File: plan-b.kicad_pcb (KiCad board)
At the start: 4 copper layers, 82.4 x 70 mm, 77 parts, among them J1 HRO_TYPE-C-31-M-14, J2 Battery, J3 rgb, J4 columns, J5 Conn_01x10, J6 rows, J7 sensor, J8 Conn_ARM_SWD_TagConnect_TC203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, J9 Conn_01x05_Pin, J99 rows, SW1 Battery, SW2 Reset, U1 nRF52840-QIAA, U3 TPS22919DCKR, U4 TPS22919DCKR, X1 32MHz, X2 32.768kHz

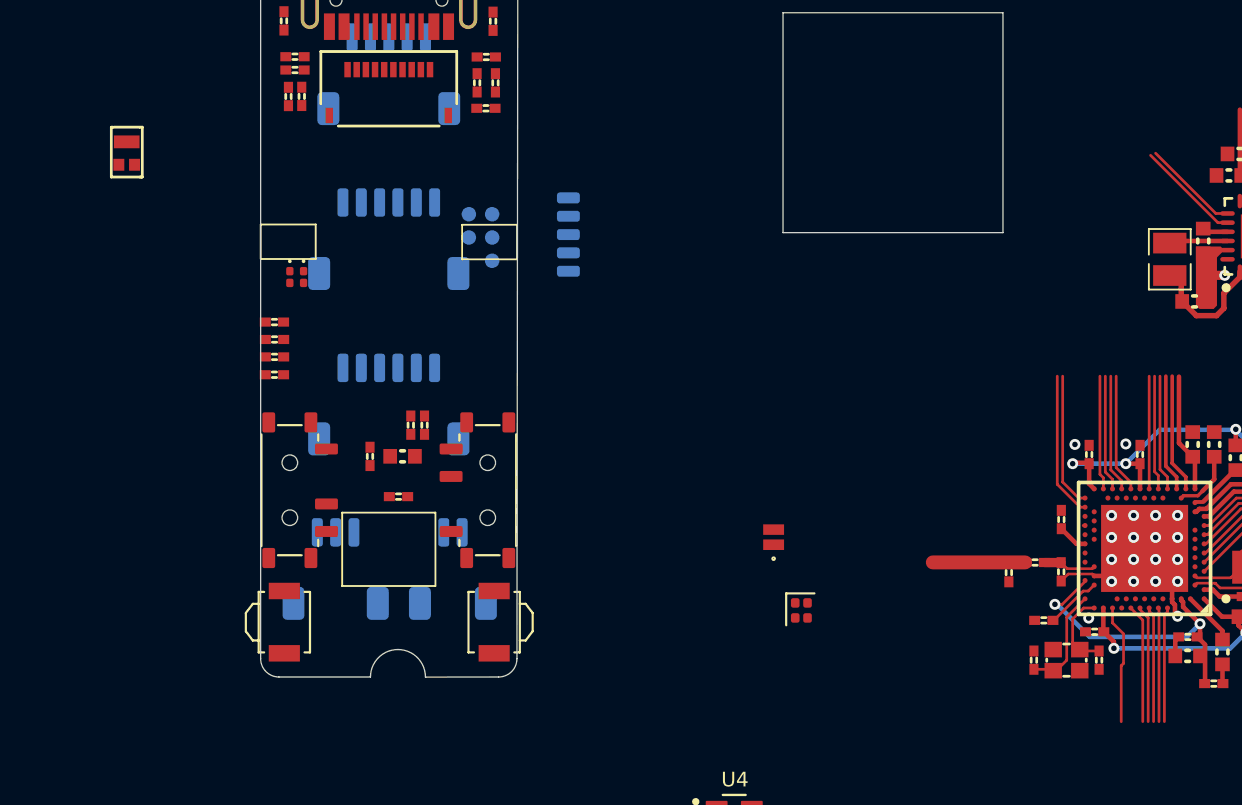
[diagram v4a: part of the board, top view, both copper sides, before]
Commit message: Setting up the RF/Antenna setup
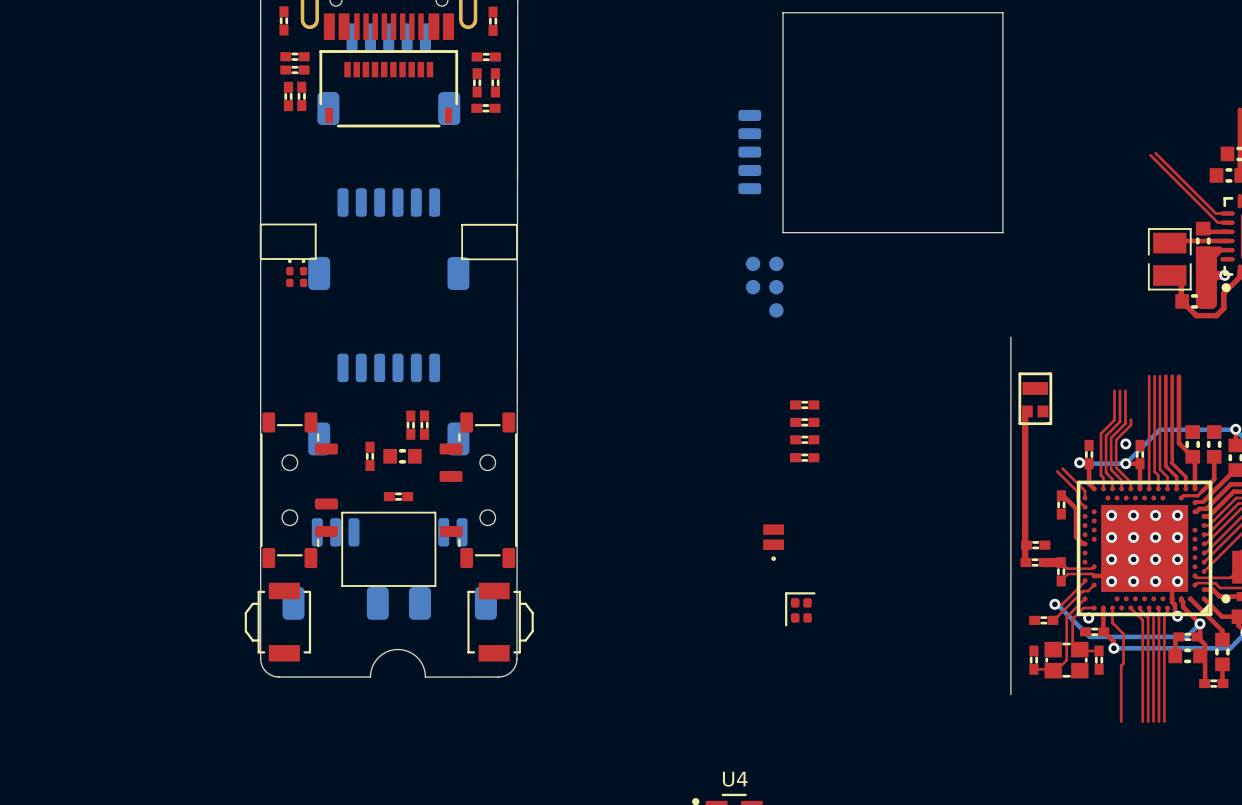
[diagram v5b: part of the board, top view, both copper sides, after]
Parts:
- moved AE1 51.4 mm to (185.3, 84.6)
- moved R11 29.3 mm to (172.7, 84.9)
- moved R14 29.3 mm to (172.7, 85.8)
- moved R15 29.3 mm to (172.7, 86.8)
- moved R16 29.3 mm to (172.7, 87.7)
- moved J8 15.7 mm to (170.5, 78.4)
- moved J9 10.9 mm to (171.4, 71.0)
- moved C4 2.09 mm to (185.3, 92.5), turned to 180 degrees
- moved C9 0.80 mm to (186.7, 90.3), turned to -90 degrees
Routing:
- net SWCLK: track 7.93 -> 2.58 mm
- net SWDIO: track 7.36 -> 2.11 mm
- net /MCU/RF: track 5.04 -> 8.29 mm
- net unconnected-(U1-P0.20-PadAD16): track 6.48 -> 4.44 mm
- net Net-(U1-DEC5): track 1.64 -> 3.39 mm
- net VDD: track 49.1 -> 48.4 mm
- net unconnected-(U1-P1.00-PadAD22): track 6.23 -> 5.71 mm
- net unconnected-(U1-P0.24-PadAD20): track 6.31 -> 5.81 mm
- net GND: vias 26 -> 25
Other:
- outline, holes or cut-outs redrawn

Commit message: Tidying up the PSU block
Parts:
- J99: value rows -> Net tie
- L5: footprint Parts$:INDC2016X10N -> Library:L_0603_1608
- U2: renamed from U1; value nRF52840-QIAA -> nPM1100-QDAx
- moved R3 1.97 mm to (201.0, 72.5), turned to 90 degrees
- moved LD2 1.93 mm to (201.1, 78.3), turned to -90 degrees
- moved R_ICHG 1.45 mm to (201.0, 74.5), turned to 90 degrees
- moved C26 1.00 mm to (193.9, 78.2)
- moved L5 0.84 mm to (193.2, 76.3)
- moved C24 0.13 mm to (196.0, 72.3)
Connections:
- J99 pad 1: Row 0 -> GND
- J99 pad 2: Row 1 -> PVSS
- U2 pad 1: (no net) -> 1.8v
- U2 pad 10: (no net) -> unconnected-(U2-ERR-Pad10)
- U2 pad 11: (no net) -> GND
- U2 pad 12: (no net) -> Net-(U2-ICHG)
- U2 pad 13: (no net) -> unconnected-(U2-NC-Pad13)
- U2 pad 14: (no net) -> Net-(U2-NTC)
- U2 pad 15: (no net) -> VBAT
- U2 pad 16: (no net) -> VSYS
- U2 pad 17: (no net) -> VBUS
- U2 pad 18: (no net) -> unconnected-(U2-NC-Pad18)
- U2 pad 19: (no net) -> D-
- U2 pad 2: (no net) -> GND
- U2 pad 20: (no net) -> D+
- U2 pad 21: (no net) -> Net-(U2-DEC)
- U2 pad 22: (no net) -> Net-(U2-SW)
- U2 pad 23: (no net) -> PVSS
- U2 pad 24: (no net) -> unconnected-(U2-NC-Pad24)
- U2 pad 25: (no net) -> GND
- U2 pad 3: (no net) -> GND
- U2 pad 4: (no net) -> GND
- U2 pad 5: (no net) -> GND
- U2 pad 6: (no net) -> GND
- U2 pad 7: (no net) -> GND
- U2 pad 8: (no net) -> Net-(LD2-C)
- U2 pad 9: (no net) -> unconnected-(U2-VTERM-Pad9)
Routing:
- net (no net): track 11.0 -> 0.00 mm
- net D+: track 6.39 -> 12.1 mm
- net D-: track 6.46 -> 11.7 mm
- net VSYS: track 29.8 -> 27.0 mm
- net 1.8v: track 7.18 -> 5.98 mm
- net Net-(U2-ICHG): track 1.55 -> 0.58 mm
- net Net-(U2-SW): track 2.84 -> 2.17 mm
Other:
- board size 82.4 x 70 mm -> 40.9 x 43 mm

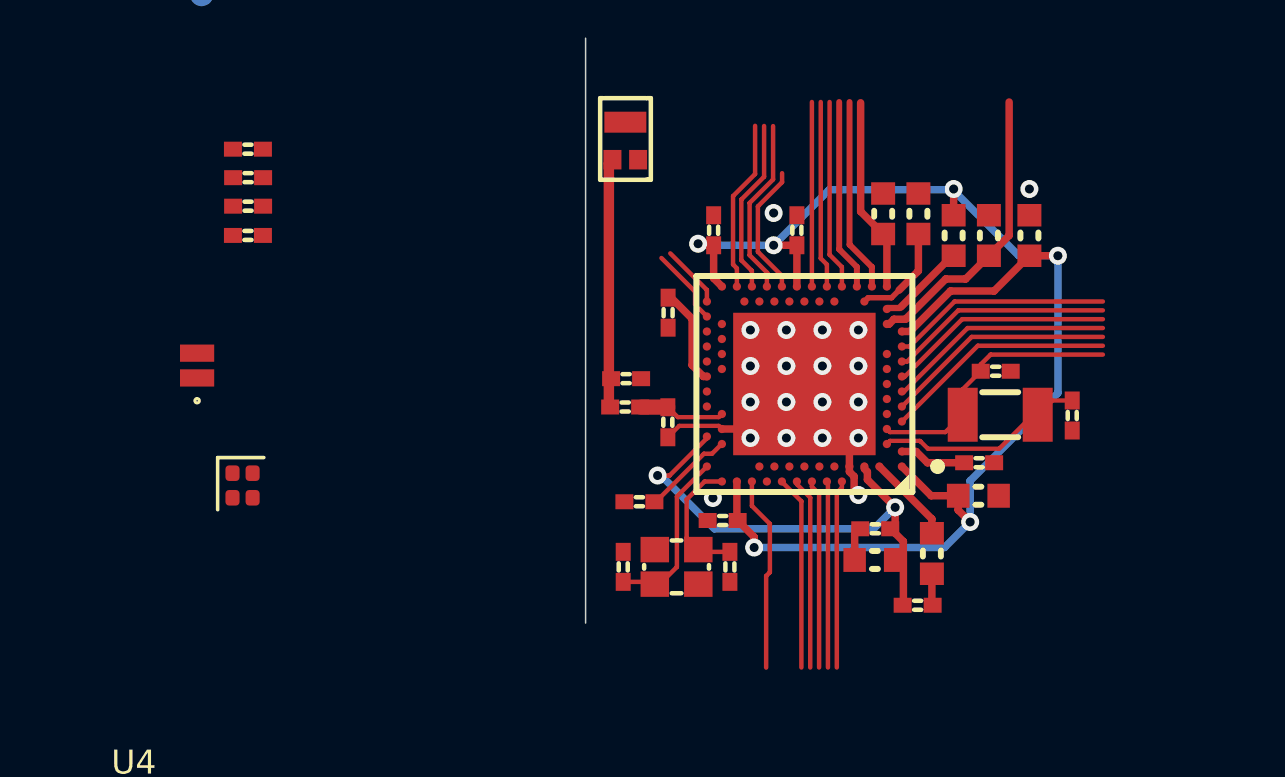
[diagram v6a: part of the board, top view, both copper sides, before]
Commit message: Switching to smaller crystalls
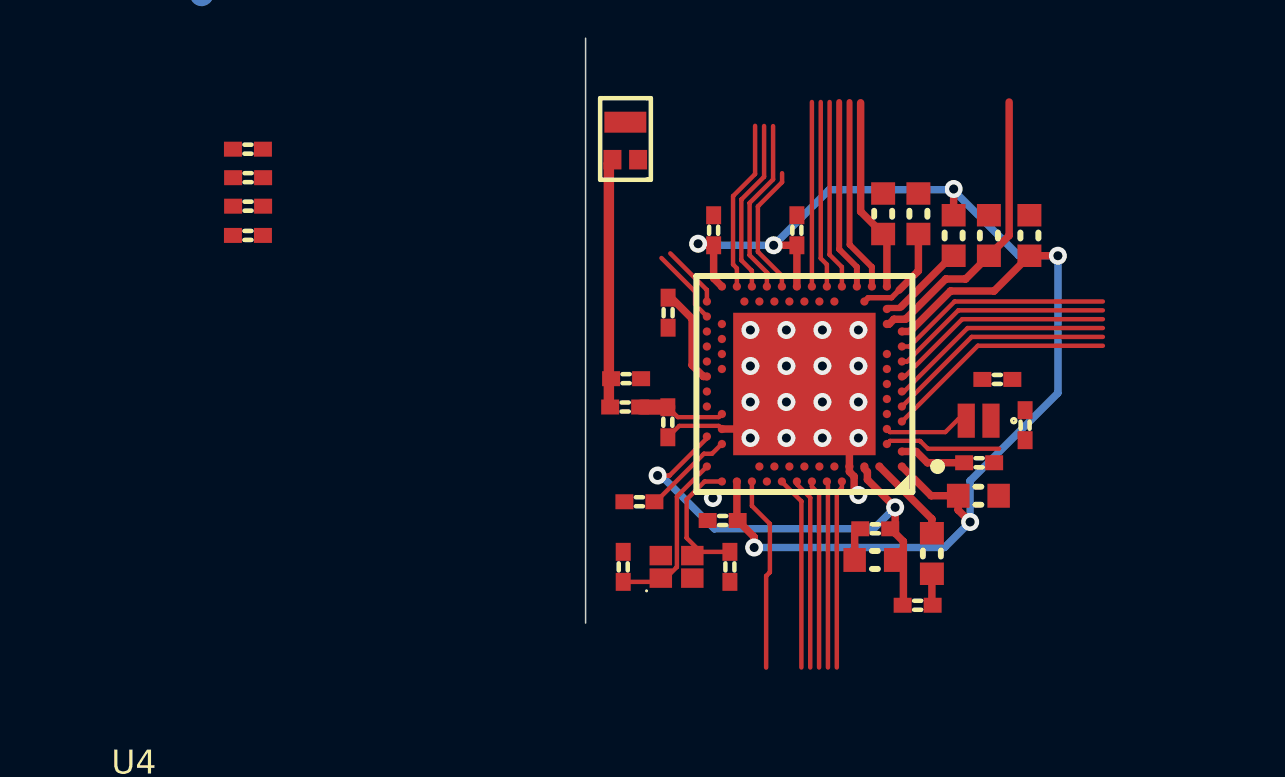
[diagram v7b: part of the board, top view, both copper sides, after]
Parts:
- removed the X1 at (172.5, 96.1)
- removed the X2 at (197.8, 93.7)
- X1: footprint Crystal_Osc$:BT-XTAL_2016 -> NX1612SA-32.000MHZ-CHP:OSCSC105P160X120X35-4N
- moved X2 26.1 mm to (197.1, 93.9), turned to 180 degrees
- moved C17 1.60 mm to (198.6, 94.0)
- moved C18 0.28 mm to (197.7, 92.5)
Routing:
- net Net-(U1-P0.01/XL2): track 8.94 -> 2.83 mm
- net Net-(U1-P0.00/XL1): track 7.00 -> 3.89 mm
- net GND: vias 25 -> 23

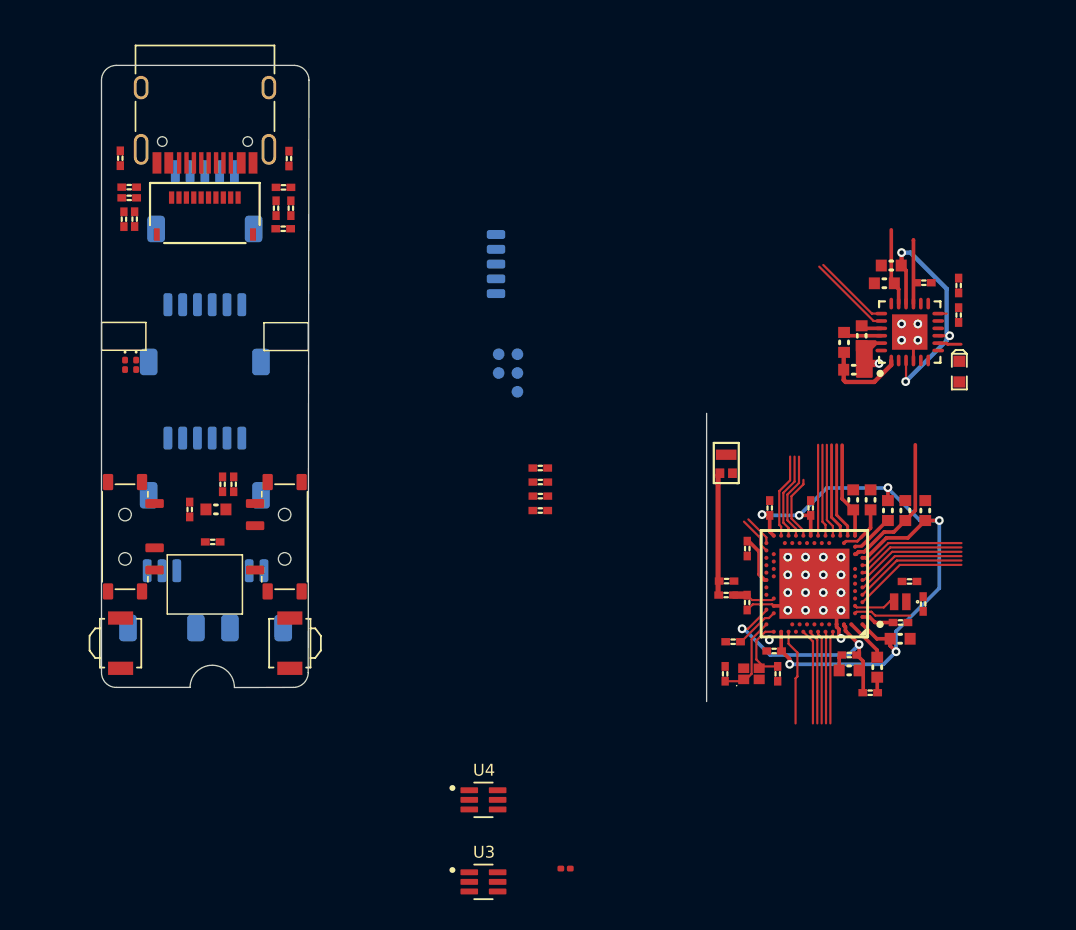
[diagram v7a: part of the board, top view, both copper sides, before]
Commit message: Sorting out the remaining components footprints and rough positioning
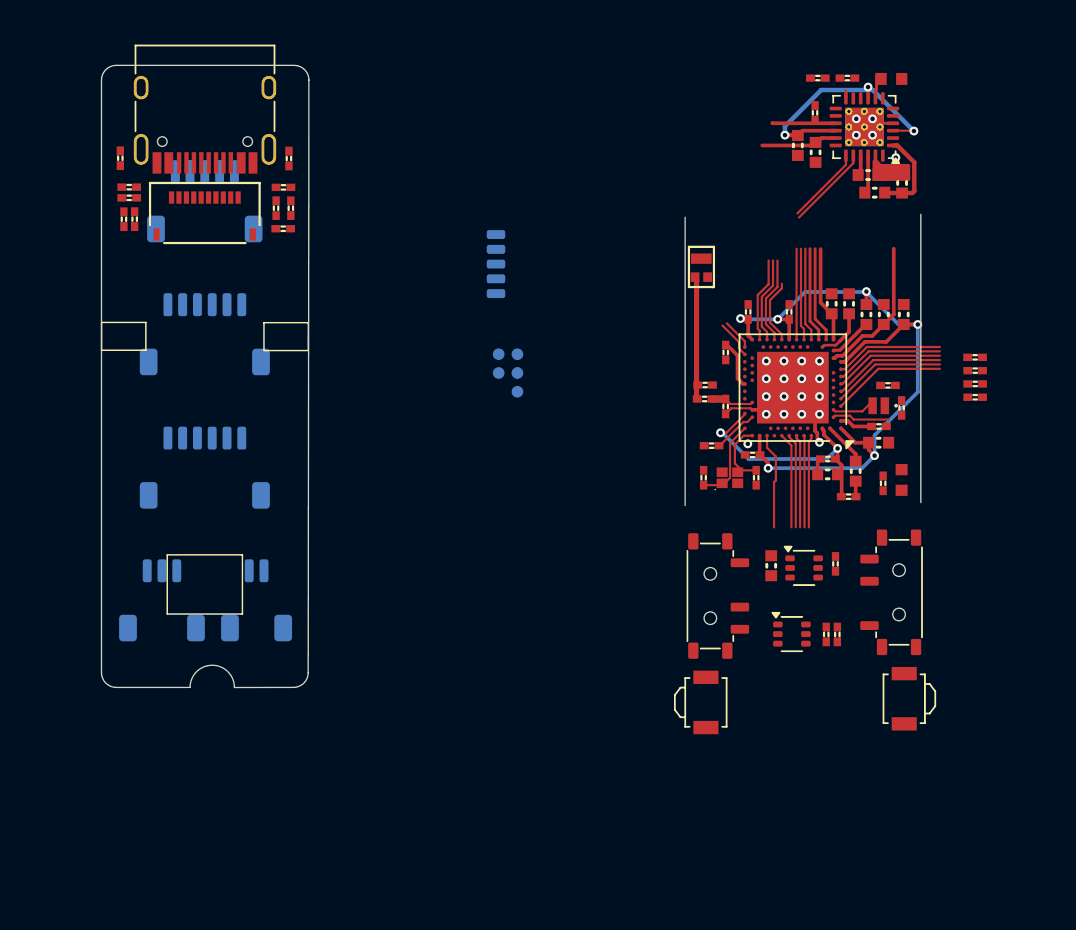
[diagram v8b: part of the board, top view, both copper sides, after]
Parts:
- removed the C22 at (150.5, 89.8)
- removed the LD2 at (145.3, 77.9)
- LD2: footprint pcblib:LED_0603_G -> Library:LED_0603_1608
- LD3: footprint LED_SMD:LED_0201_0603Metric -> Library:LED_0603_1608
- R_BLE1: footprint Resistor_SMD:R_0201_0603Metric -> Library:R_0402_1005
- U1: footprint AQFN50P700X700X85_HS-74N:AQFN50P700X700X85_HS-74N -> Package_DFN_QFN:Nordic_AQFN-73-1EP_7x7mm_P0.5mm
- U2: footprint Parts$:QFN50P400X400X80_HS-25N -> Package_DFN_QFN:QFN-24-1EP_4x4mm_P0.5mm_EP2.6x2.6mm_ThermalVias
- U3, U4: footprint TPS22919:SOT65P210X110-6N -> Package_TO_SOT_SMD:SOT-363_SC-70-6
- moved LD3 53.1 mm to (197.1, 85.7), turned to 90 degrees
- moved R8 43.8 mm to (192.7, 91.3)
- moved R_DIV1 42.1 mm to (192.8, 96.1)
- moved R_DIV2 42.1 mm to (192.0, 96.1)
- moved SW1 41.7 mm to (197.0, 93.3)
- moved SW2 41.7 mm to (197.3, 100.5)
- moved SW1 39.8 mm to (184.2, 93.5)
- moved SW2 39.8 mm to (183.9, 100.7)
- moved C44 37.8 mm to (188.3, 91.5), turned to 90 degrees
- moved R_BLE1 33.8 mm to (195.9, 85.9), turned to 90 degrees
- moved R16 30.4 mm to (202.1, 80.1)
- moved R15 30.4 mm to (202.1, 79.2)
- moved R14 30.4 mm to (202.1, 78.3)
- moved R11 30.4 mm to (202.1, 77.4)
- moved U4 26.8 mm to (190.5, 91.6)
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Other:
- board size 40.9 x 43 mm -> 55.4 x 42.1 mm
